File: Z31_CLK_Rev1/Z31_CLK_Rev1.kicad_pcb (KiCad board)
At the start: 2 copper layers, 74 x 50 mm, 16 parts, among them J1 Conn_01x06_Male, J2 ICSP, U1 MAX6922, U2 4BT-78Z_6L, U3 ATMEGA328-AURCT-ND, U4 MCP2510, U5 TJR1443, Y1 8MHz, Y2 16MHz

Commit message: add code
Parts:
- removed C4: 100n, Capacitor_SMD:C_0805_2012Metric_Pad1.18x1.45mm_HandSolder
- removed U1: MAX6922, Package_LCC:PLCC-44_16.6x16.6mm_P1.27mm
- removed U2: 4BT-78Z_6L, Personal:4BT-78Z_6L

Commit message: Catchup
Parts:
- removed the C3 at (128.9, 50.2)
- removed the Y1 at (97.0, 61.0)
- added C1: 100nF, Capacitor_SMD:C_0805_2012Metric_Pad1.18x1.45mm_HandSolder, F.Cu at (116.0, 41.1)
- added C10: 100nF, Capacitor_SMD:C_0805_2012Metric_Pad1.18x1.45mm_HandSolder, F.Cu at (122.4, 35.1)
- added C11: 22uF, Capacitor_SMD:CP_Elec_5x5.7, F.Cu at (101.1, 41.2)
- added C12: N/A, Capacitor_SMD:C_0805_2012Metric_Pad1.18x1.45mm_HandSolder, F.Cu at (116.0, 44.1)
- added C13: yes, Capacitor_SMD:C_1210_3225Metric_Pad1.33x2.70mm_HandSolder, F.Cu at (125.7, 25.8)
- added C4: 10pF, Capacitor_SMD:C_0805_2012Metric_Pad1.18x1.45mm_HandSolder, F.Cu at (131.2, 28.6)
- added C8: 100nF, Capacitor_SMD:C_0805_2012Metric_Pad1.18x1.45mm_HandSolder, F.Cu at (122.4, 38.1)
- added C9: 1u, Capacitor_SMD:C_1210_3225Metric_Pad1.33x2.70mm_HandSolder, F.Cu at (123.0, 31.5)
- added D1: D_Schottky, Diode_SMD:D_SMA, F.Cu at (109.6, 41.8)
- added D2: SMAJ18CAQ-13-F, Diode_SMD:D_SMA, F.Cu at (126.8, 21.4)
- added F1: Polyfuse, Fuse:Fuse_1812_4532Metric_Pad1.30x3.40mm_HandSolder, F.Cu at (134.4, 21.6)
- added R1: 47K, Resistor_SMD:R_0805_2012Metric_Pad1.20x1.40mm_HandSolder, F.Cu at (120.8, 44.1)
- added R2: R, Resistor_SMD:R_0805_2012Metric_Pad1.20x1.40mm_HandSolder, F.Cu at (127.2, 35.1)
- added R3: R, Resistor_SMD:R_0805_2012Metric_Pad1.20x1.40mm_HandSolder, F.Cu at (135.9, 28.6)
- added R4: 10k, Resistor_SMD:R_0805_2012Metric_Pad1.20x1.40mm_HandSolder, F.Cu at (133.1, 31.6)
- added R5: N/A, Resistor_SMD:R_0805_2012Metric_Pad1.20x1.40mm_HandSolder, F.Cu at (127.2, 38.1)
- added R6: N/A, Resistor_SMD:R_0805_2012Metric_Pad1.20x1.40mm_HandSolder, F.Cu at (120.8, 41.1)
- added TH1: NTC 47K, Resistor_SMD:R_0805_2012Metric_Pad1.20x1.40mm_HandSolder, F.Cu at (128.4, 31.6)
- added U3: MCP2515-xST, Package_SO:TSSOP-20_4.4x6.5mm_P0.65mm, F.Cu at (115.6, 35.5)
- added Y2: 8MHz, Crystal:Crystal_SMD_HC49-SD, F.Cu at (103.9, 34.6)
- C2: value 100n -> 100nF
- C5: value 100n -> 10pF
- C6, C7: value 20p -> 100nF
- U4: value MCP2510 -> TJR1443; footprint Package_SO:TSSOP-20_4.4x6.5mm_P0.65mm -> Package_SO:SO-14_3.9x8.65mm_P1.27mm; moved to F.Cu
- U5: value TJR1443 -> NCV4276B; footprint Package_SO:SO-14_3.9x8.65mm_P1.27mm -> Package_TO_SOT_SMD:TO-263-5_TabPin3; moved to F.Cu
- moved C6 86.4 mm to (185.3, 68.7)
- moved C7 64.2 mm to (140.5, 20.7)
- moved U4 59.8 mm to (118.5, 24.3), turned to 0 degrees
- moved U5 46.7 mm to (105.4, 25.3), turned to 0 degrees
- moved C2 29.0 mm to (131.2, 25.6)
- moved C5 27.3 mm to (136.0, 25.6)
- renumbered C1 to C3, J2 to J1, J1 to J2, U3 to U1, Y2 to Y1
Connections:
- C2 pad 1: +5V -> /MODULE_VOLTAGE
- C5 pad 1: Net-(C5-Pad1) -> GND
- C5 pad 2: GND -> Net-(C5-Pad2)
- C6 pad 2: Net-(C6-Pad2) -> +5V
- C7 pad 2: Net-(C7-Pad2) -> +5V
- U1 pad 14: CS_CAN -> /CS_CAN
- U1 pad 19: unconnected-(U3-Pad19) -> /MODULE_TEMPERATURE
- U1 pad 20: Net-(C5-Pad1) -> unconnected-(U1-Pad20)
- U1 pad 22: unconnected-(U3-Pad22) -> /MODULE_VOLTAGE
- U1 pad 9: VFBLANK -> unconnected-(U1-Pad9)
- U4 pad 1: Net-(U4-Pad1) -> /TXCAN
- U4 pad 10: GND -> +12V
- U4 pad 11: Net-(U4-Pad11) -> unconnected-(U4-Pad11)
- U4 pad 12: Net-(U4-Pad12) -> CANL
- U4 pad 13: CAN_INT -> CANH
- U4 pad 14: SCK -> /CAN_STB
- U4 pad 2: Net-(U4-Pad2) -> GND
- U4 pad 3: unconnected-(U4-Pad3) -> +5V
- U4 pad 4: unconnected-(U4-Pad4) -> /RXCAN
- U4 pad 5: unconnected-(U4-Pad5) -> +5V
- U4 pad 6: unconnected-(U4-Pad6) -> /CAN_EN
- U4 pad 7: unconnected-(U4-Pad7) -> Net-(R4-Pad1)
- U4 pad 8: Net-(C6-Pad2) -> /CAN_ERR
- U4 pad 9: Net-(C7-Pad2) -> /MODULE_VOLTAGE
- U5 pad 1: Net-(U4-Pad1) -> +12V
- U5 pad 2: unconnected-(U5-Pad2) -> Net-(R4-Pad1)
- U5 pad 3: +5V -> GND
- U5 pad 4: Net-(U4-Pad2) -> Net-(C12-Pad2)

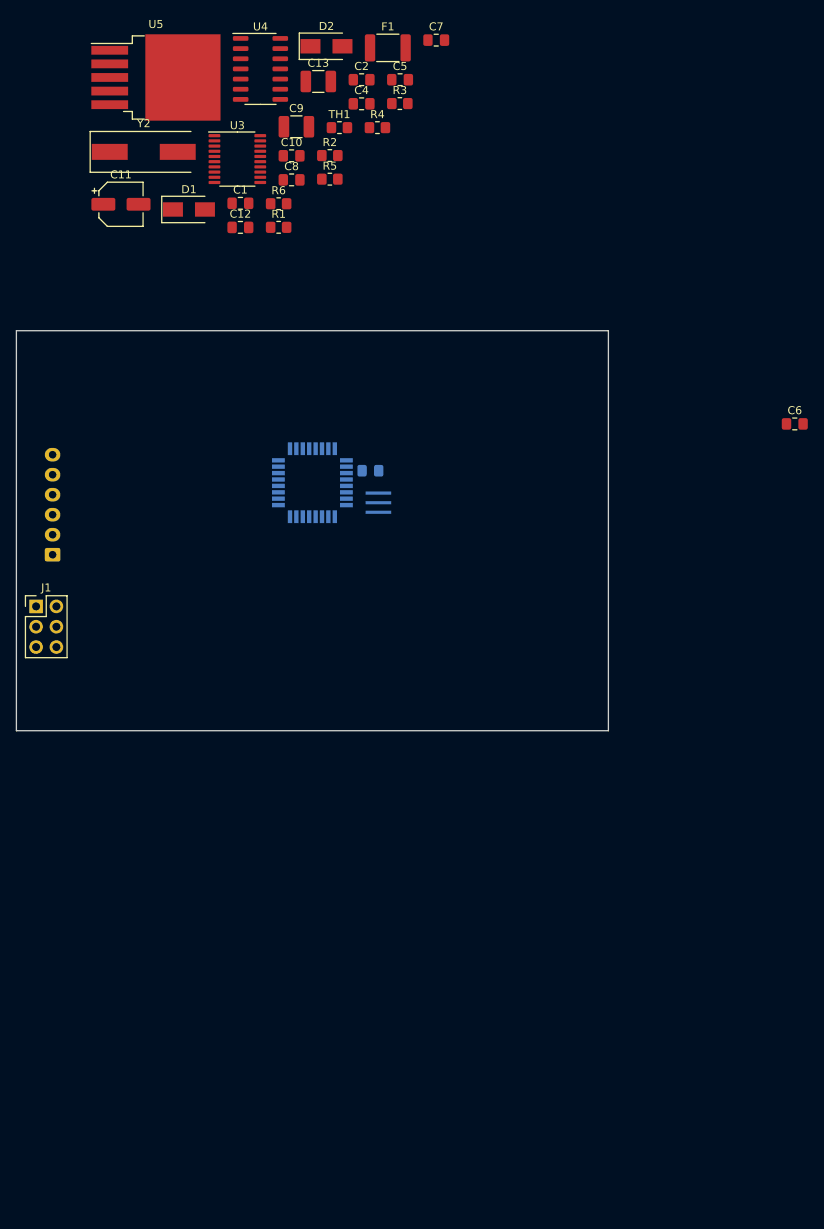
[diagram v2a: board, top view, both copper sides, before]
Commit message: Feature-complete Z31-CLK-Rev1; some PCB layout cleanup may still be useful.
Review pending.
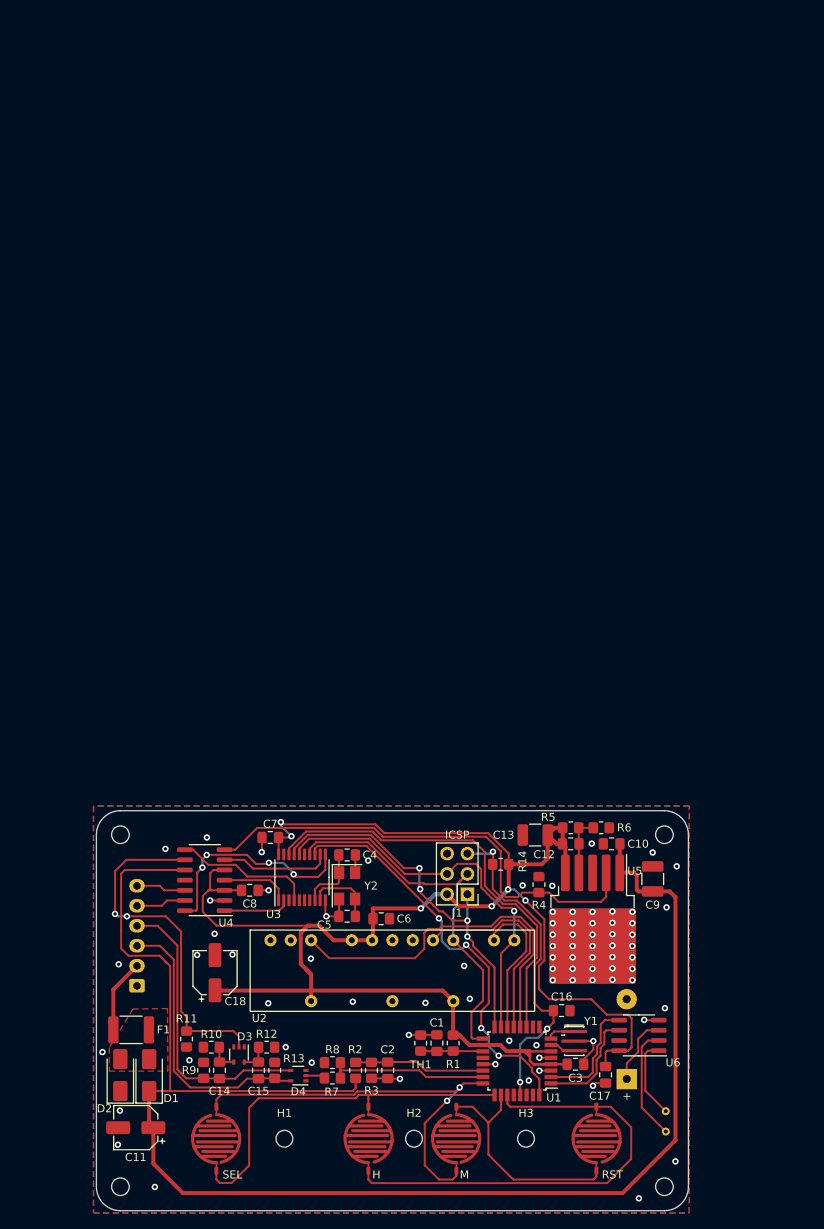
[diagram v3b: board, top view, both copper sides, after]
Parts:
- added BT1: 3V, Battery:BatteryHolder_Keystone_500, B.Cu at (164.3, 150.5)
- added C14: 100n, Capacitor_SMD:C_0805_2012Metric_Pad1.18x1.45mm_HandSolder, F.Cu at (113.4, 149.5)
- added C15: 100n, Capacitor_SMD:C_0805_2012Metric_Pad1.18x1.45mm_HandSolder, F.Cu at (118.3, 149.5)
- added C16: 100nF, Capacitor_SMD:C_0805_2012Metric_Pad1.18x1.45mm_HandSolder, F.Cu at (156.2, 142.0)
- added C17: 100nF, Capacitor_SMD:C_0805_2012Metric_Pad1.18x1.45mm_HandSolder, F.Cu at (161.6, 150.0)
- added C18: 22uF, Capacitor_SMD:CP_Elec_5x5.7, F.Cu at (112.8, 137.2)
- added D3: MMBD4448HCQW, Package_TO_SOT_SMD:SOT-353_SC-70-5, F.Cu at (115.8, 147.5)
- added D4: MMBD4448HCQW, Package_TO_SOT_SMD:SOT-353_SC-70-5, F.Cu at (123.2, 150.1)
- added H1: MountingHole, MountingHole:MountingHole_2.1mm, F.Cu at (121.5, 158.0)
- added H2: MountingHole, MountingHole:MountingHole_2.1mm, F.Cu at (137.7, 158.0)
- added H3: MountingHole, MountingHole:MountingHole_2.1mm, F.Cu at (151.7, 158.0)
- added H4: MountingHole, MountingHole:MountingHole_2.2mm_M2_DIN965, F.Cu at (101.0, 120.0)
- added H5: MountingHole, MountingHole:MountingHole_2.2mm_M2_DIN965, F.Cu at (169.0, 120.0)
- added H6: MountingHole, MountingHole:MountingHole_2.2mm_M2_DIN965, F.Cu at (169.0, 164.0)
- added H7: MountingHole, MountingHole:MountingHole_2.2mm_M2_DIN965, F.Cu at (101.0, 164.0)
- added R10: 10k, Resistor_SMD:R_0805_2012Metric_Pad1.20x1.40mm_HandSolder, F.Cu at (112.4, 146.6)
- added R11: 10k, Resistor_SMD:R_0805_2012Metric_Pad1.20x1.40mm_HandSolder, F.Cu at (109.3, 145.5)
- added R12: 10k, Resistor_SMD:R_0805_2012Metric_Pad1.20x1.40mm_HandSolder, F.Cu at (119.3, 146.6)
- added R13: 10k, Resistor_SMD:R_0805_2012Metric_Pad1.20x1.40mm_HandSolder, F.Cu at (120.3, 149.5)
- added R14: 10k, Resistor_SMD:R_0805_2012Metric_Pad1.20x1.40mm_HandSolder, F.Cu at (148.5, 123.7)
- added R7: 10k, Resistor_SMD:R_0805_2012Metric_Pad1.20x1.40mm_HandSolder, F.Cu at (127.5, 150.4)
- added R8: 10k, Resistor_SMD:R_0805_2012Metric_Pad1.20x1.40mm_HandSolder, F.Cu at (127.5, 148.5)
- added R9: 10k, Resistor_SMD:R_0805_2012Metric_Pad1.20x1.40mm_HandSolder, F.Cu at (111.4, 149.5)
- added SW1: Select, Personal:membrane_button, F.Cu at (113.0, 158.0)
- added SW2: Hour, Personal:membrane_button, F.Cu at (132.0, 158.0)
- added SW3: Reset, Personal:membrane_button, F.Cu at (143.0, 158.0)
- added SW4: Minute, Personal:membrane_button, F.Cu at (160.5, 158.0)
- added U2: HCMS-291x, Personal:HCMS-291x, F.Cu at (135.0, 137.0)
- added U6: DS1307Z+, Package_SO:SOIC-8_3.9x4.9mm_P1.27mm, F.Cu at (165.8, 145.1)
- added Y3: 32.768k, Crystal:Crystal_AT310_D3.0mm_L10.0mm_Horizontal, B.Cu at (169.2, 157.1)
- C3, U1, Y1: moved to F.Cu
- Y2: footprint Crystal:Crystal_SMD_HC49-SD -> Crystal:Crystal_SMD_5032-4Pin_5.0x3.2mm
- moved D2 131.2 mm to (101.0, 150.0), turned to 90 degrees
- moved F1 126.9 mm to (102.3, 144.4), turned to 180 degrees
- moved C2 123.9 mm to (134.4, 149.5), turned to -90 degrees
- moved R3 120.9 mm to (132.4, 149.5), turned to -90 degrees
- moved U5 120.2 mm to (160.0, 132.4), turned to -90 degrees
- moved C11 115.4 mm to (102.9, 156.6), turned to 180 degrees
- moved TH1 114.9 mm to (138.5, 146.1), turned to 90 degrees
- moved R2 114.4 mm to (130.4, 149.5), turned to 90 degrees
- moved D1 108.3 mm to (104.6, 150.0), turned to 90 degrees
- moved C1 107.8 mm to (140.6, 146.1), turned to 90 degrees
- moved C5 104.8 mm to (129.3, 130.2)
- moved R1 104.3 mm to (142.6, 146.1), turned to -90 degrees
- moved C9 104.0 mm to (167.5, 125.5), turned to 90 degrees
- moved C7 101.8 mm to (119.7, 120.3)
- moved U4 101.6 mm to (111.5, 125.7), turned to 180 degrees
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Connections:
- net CANH renamed /CANH
- net CANL renamed /CANL
- net Net-(R4-Pad1) renamed /~{INH}
- C4 pad 2: Net-(C4-Pad2) -> Net-(U3-OSC2)
- C5 pad 2: Net-(C5-Pad2) -> Net-(U3-OSC1)
- F1 pad 2: +12V_CONST -> /+12V_CONST
- J2 pad 2: ILLUM -> /+12V_CONST
- J2 pad 3: +12V_CONST -> /ILLUM
- J2 pad 4: +12V_ACC -> /+12V_ACC
- R2 pad 1: /+12V_IGN -> +12V
- U1 pad 1: unconnected-(U1-Pad1) -> Net-(U1-PD3)
- U1 pad 11: unconnected-(U1-Pad11) -> /~{CS_CAN}
- U1 pad 12: unconnected-(U1-Pad12) -> /~{RST_DISP}
- U1 pad 13: CS_DISP -> /~{CS_DISP}
- U1 pad 14: /CS_CAN -> /RS_DISP
- U1 pad 18: unconnected-(U1-Pad18) -> +5V
- U1 pad 2: unconnected-(U1-Pad2) -> Net-(U1-PD4)
- U1 pad 23: unconnected-(U1-Pad23) -> /Wake_Sense
- U1 pad 24: unconnected-(U1-Pad24) -> /Key_A
- U1 pad 25: unconnected-(U1-Pad25) -> /Key_2
- U1 pad 26: unconnected-(U1-Pad26) -> /Key_1
- U1 pad 27: unconnected-(U1-Pad27) -> /Key_B
- U1 pad 29: unconnected-(U1-Pad29) -> RESET
- U1 pad 30: unconnected-(U1-Pad30) -> RXD
- U1 pad 31: unconnected-(U1-Pad31) -> TXD
- U3 pad 18: /CS_CAN -> /~{CS_CAN}
- U3 pad 19: /RESET_CAN -> unconnected-(U3-~{RESET}-Pad19)
- U3 pad 8: Net-(C4-Pad2) -> Net-(U3-OSC2)
- U3 pad 9: Net-(C5-Pad2) -> Net-(U3-OSC1)
- U4 pad 1: /TXCAN -> /RXCAN
- U4 pad 4: /RXCAN -> /TXCAN
- U4 pad 9: /MODULE_VOLTAGE -> /Wake_Pulse
- Y2 pad 1: Net-(C5-Pad2) -> Net-(U3-OSC2)
- Y2 pad 2: Net-(C4-Pad2) -> GND
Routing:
- net +5V: track 0.00 -> 225.4 mm, vias 0 -> 6
- net +12V: track 0.00 -> 189.5 mm
- net /~{INH}: track 0.00 -> 59.4 mm
- net /Key_B: track 0.00 -> 57.1 mm
- net /~{CS_CAN}: track 0.00 -> 53.4 mm
- net /Key_A: track 0.00 -> 52.1 mm, vias 0 -> 2
- net CAN_INT: track 0.00 -> 51.7 mm, vias 0 -> 4
- net MOSI: track 0.00 -> 49.5 mm, vias 0 -> 1
- net SCK: track 0.00 -> 48.3 mm
- net MISO: track 0.00 -> 47.9 mm, vias 0 -> 4
- net /Key_2: track 0.00 -> 46.3 mm
- net /~{RST_DISP}: track 0.00 -> 45.5 mm
- net /Wake_Pulse: track 0.00 -> 44.7 mm, vias 0 -> 2
- net RESET: track 0.00 -> 41.8 mm, vias 0 -> 3
- net /+12V_ACC: track 0.00 -> 36.6 mm
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- added copper zone on B.Cu, net GND
- added copper zone on F.Cu, net GND
- added copper zone on F.Cu, net Net-(D1-A)
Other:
- outline, holes or cut-outs redrawn
- board text added: "Z31-CLK-Rev 1 A.M. 2025"

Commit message: Finalize clock design
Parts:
- moved C7 1.27 mm to (119.7, 121.6)
- moved U3 1.22 mm to (123.7, 126.5)
- moved C8 1.02 mm to (116.4, 127.7), turned to 90 degrees
- moved C5 0.66 mm to (129.3, 130.9)
- moved C4 0.66 mm to (129.3, 123.2)
- moved Y2 0.66 mm to (129.3, 127.1)
- moved F1 0.58 mm to (102.3, 143.8)
- turned C18 to -90 degrees
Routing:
- net +5V: track 225.4 -> 236.5 mm, vias 6 -> 8
- net GND: track 33.9 -> 37.9 mm, vias 79 -> 98
- net +12V: track 189.5 -> 190.3 mm
- net /~{RST_DISP}: track 45.5 -> 44.8 mm
- net /~{CS_CAN}: track 53.4 -> 54.1 mm
- net MISO: track 47.9 -> 48.6 mm
- net SCK: track 48.3 -> 48.8 mm
- net /CAN_EN: track 13.8 -> 14.4 mm
- net MOSI: track 49.5 -> 50.0 mm
